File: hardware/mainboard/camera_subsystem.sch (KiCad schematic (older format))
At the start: 12 parts

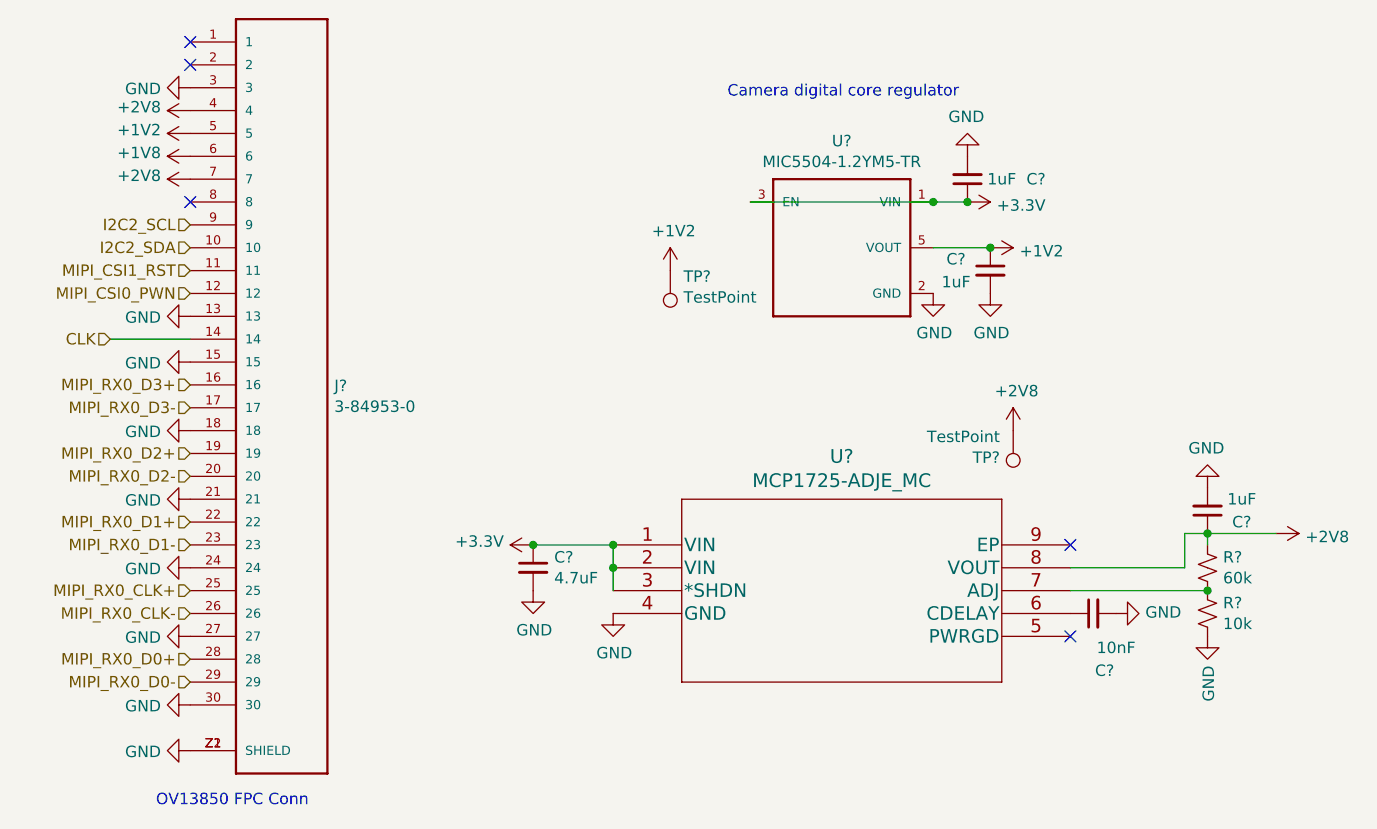
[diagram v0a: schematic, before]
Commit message: finish sch arch, remove coproc, add bl driver, need to do TC power supply
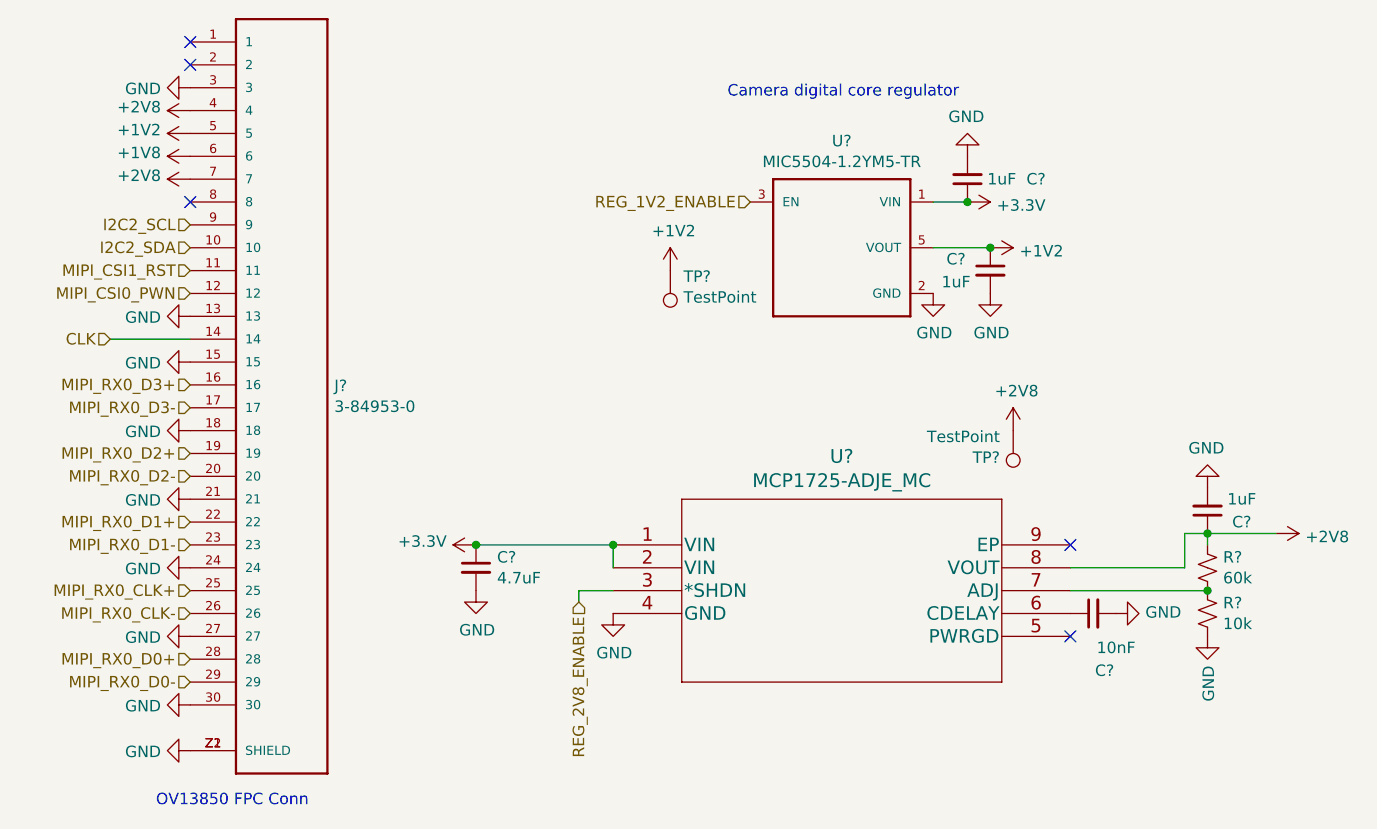
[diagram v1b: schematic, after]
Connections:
- net +3V3: no longer U?.3 (*SHDN), U?.3 (EN)
- new net REG_1V2_ENABLE: U?.3 (EN)
- new net REG_2V8_ENABLE: U?.3 (*SHDN)
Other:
- moved on the sheet: C?
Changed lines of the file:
@@
 	1    0    0    -1
 $EndComp
-Connection ~ 6150 1900
-Wire Wire Line
-	5350 1900 6150 1900
 $Comp
 L power:GND #PWR?
@@
 L power:GND #PWR?
 U 1 1 600090EF
-P 4400 3600
+P 4150 3600
 AR Path="/600090EF" Ref="#PWR?"  Part="1"
 AR Path="/5FFAA2CE/600090EF" Ref="#PWR?"  Part="1"
-F 0 "#PWR?" H 4400 3350 50  0001 C CNN
-F 1 "GND" H 4405 3427 50  0000 C CNN
-F 2 "" H 4400 3600 50  0001 C CNN
-F 3 "" H 4400 3600 50  0001 C CNN
-	1    4400 3600
+F 0 "#PWR?" H 4150 3350 50  0001 C CNN
+F 1 "GND" H 4155 3427 50  0000 C CNN
+F 2 "" H 4150 3600 50  0001 C CNN
+F 3 "" H 4150 3600 50  0001 C CNN
+	1    4150 3600
 	1    0    0    -1
 $EndComp
@@
 L Device:C_Small C?
 U 1 1 600090F5
-P 4400 3500
+P 4150 3500
 AR Path="/600090F5" Ref="C?"  Part="1"
 AR Path="/5FFAA2CE/600090F5" Ref="C?"  Part="1"
-F 0 "C?" H 4492 3546 50  0000 L CNN
-F 1 "4.7uF" H 4492 3455 50  0000 L CNN
-F 2 "Capacitor_SMD:C_0402_1005Metric_Pad0.74x0.62mm_HandSolder" H 4400 3500 50  0001 C CNN
-F 3 "~" H 4400 3500 50  0001 C CNN
-	1    4400 3500
+F 0 "C?" H 4242 3546 50  0000 L CNN
+F 1 "4.7uF" H 4242 3455 50  0000 L CNN
+F 2 "Capacitor_SMD:C_0402_1005Metric_Pad0.74x0.62mm_HandSolder" H 4150 3500 50  0001 C CNN
+F 3 "~" H 4150 3500 50  0001 C CNN
+	1    4150 3500
 	1    0    0    -1
 $EndComp
@@
 $EndComp
 Wire Wire Line
-	4750 3500 4750 3600
-Connection ~ 4750 3500
-Wire Wire Line
 	4750 3400 4750 3500
-$Comp
-L mainboard:MCP1725-ADJE_MC U?
-U 1 1 60009112
-P 4750 3400
-AR Path="/60009112" Ref="U?"  Part="1"
-AR Path="/5FFAA2CE/60009112" Ref="U?"  Part="1"
-F 0 "U?" H 5750 3787 60  0000 C CNN
-F 1 "MCP1725-ADJE_MC" H 5750 3681 60  0000 C CNN
-F 2 "mainboard:MCP1725-ADJE_MC" H 5750 3640 60  0001 C CNN
-F 3 "" H 4750 3400 60  0000 C CNN
-	1    4750 3400
-	1    0    0    -1
-$EndComp
 $Comp
 L power:GND #PWR?
@@
 L power:+3.3V #PWR?
 U 1 1 60009124
-P 4400 3400
+P 4150 3400
 AR Path="/60009124" Ref="#PWR?"  Part="1"
 AR Path="/5FFAA2CE/60009124" Ref="#PWR?"  Part="1"
-F 0 "#PWR?" H 4400 3250 50  0001 C CNN
-F 1 "+3.3V" V 4415 3528 50  0000 L CNN
-F 2 "" H 4400 3400 50  0001 C CNN
-F 3 "" H 4400 3400 50  0001 C CNN
-	1    4400 3400
+F 0 "#PWR?" H 4150 3250 50  0001 C CNN
+F 1 "+3.3V" V 4165 3528 50  0000 L CNN
+F 2 "" H 4150 3400 50  0001 C CNN
+F 3 "" H 4150 3400 50  0001 C CNN
+	1    4150 3400
 	0    -1   -1   0
 $EndComp
-Wire Wire Line
-	4400 3400 4750 3400
-Connection ~ 4400 3400
-Connection ~ 4750 3400
+Connection ~ 4150 3400
 Wire Wire Line
 	6750 3600 7350 3600
@@
 Text HLabel 2900 2000 0    50   Input ~ 0
 I2C2_SCL
+$Comp
+L mainboard:MCP1725-ADJE_MC U?
+U 1 1 60009112
+P 4750 3400
+AR Path="/60009112" Ref="U?"  Part="1"
+AR Path="/5FFAA2CE/60009112" Ref="U?"  Part="1"
+F 0 "U?" H 5750 3787 60  0000 C CNN
+F 1 "MCP1725-ADJE_MC" H 5750 3681 60  0000 C CNN
+F 2 "mainboard:MCP1725-ADJE_MC" H 5750 3640 60  0001 C CNN
+F 3 "" H 4750 3400 60  0000 C CNN
+	1    4750 3400
+	1    0    0    -1
+$EndComp
+Wire Wire Line
+	4150 3400 4750 3400
+Connection ~ 4750 3400
+Wire Wire Line
+	4600 3650 4600 3600
+Wire Wire Line
+	4600 3600 4750 3600
+Text HLabel 4600 3650 3    50   Input ~ 0
+REG_2V8_ENABLE
+Text HLabel 5350 1900 0    50   Input ~ 0
+REG_1V2_ENABLE
 $EndSCHEMATC

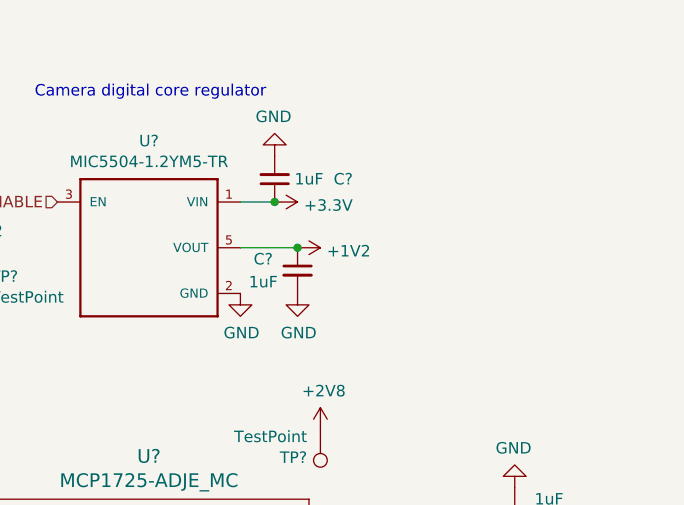
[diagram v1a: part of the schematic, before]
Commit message: finish basic schematic, need to decide audio situation
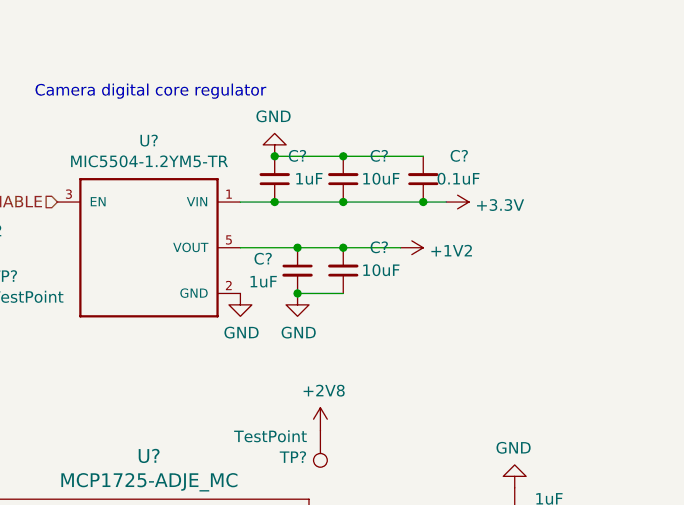
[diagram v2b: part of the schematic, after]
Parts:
- added C? (x2): 10uF, symbol Device:C_Small
- added C?: 0.1uF, symbol Device:C_Small
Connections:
- net +1V2: now also C?.2
- net +3V3: now also C?.1, C?.1
- net GND: now also C?.1, C?.2, C?.2
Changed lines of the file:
@@
 $Descr A4 11693 8268
 encoding utf-8
-Sheet 6 7
+Sheet 3 7
 Title ""
 Date ""
@@
 L power:+3.3V #PWR?
 U 1 1 5FFF5446
-P 6300 1900
+P 7050 1900
 AR Path="/5FFF5446" Ref="#PWR?"  Part="1"
 AR Path="/5FFAA2CE/5FFF5446" Ref="#PWR?"  Part="1"
-F 0 "#PWR?" H 6300 1750 50  0001 C CNN
-F 1 "+3.3V" V 6315 2028 50  0000 L CNN
-F 2 "" H 6300 1900 50  0001 C CNN
-F 3 "" H 6300 1900 50  0001 C CNN
-	1    6300 1900
+F 0 "#PWR?" H 7050 1750 50  0001 C CNN
+F 1 "+3.3V" V 7065 2028 50  0000 L CNN
+F 2 "" H 7050 1900 50  0001 C CNN
+F 3 "" H 7050 1900 50  0001 C CNN
+	1    7050 1900
 	0    1    1    0
 $EndComp
@@
 AR Path="/5FFF544C" Ref="C?"  Part="1"
 AR Path="/5FFAA2CE/5FFF544C" Ref="C?"  Part="1"
-F 0 "C?" H 6000 1800 50  0000 C CNN
+F 0 "C?" H 6200 1700 50  0000 C CNN
 F 1 "1uF" H 6150 1800 50  0000 C CNN
 F 2 "Capacitor_SMD:C_0402_1005Metric_Pad0.74x0.62mm_HandSolder" H 6300 1800 50  0001 C CNN
@@
 Wire Wire Line
 	6150 1900 6300 1900
-Connection ~ 6300 1900
 $Comp
 L power:GND #PWR?
@@
 L power:+1V2 #PWR?
 U 1 1 5FFF546D
-P 6400 2100
+P 6850 2100
 AR Path="/5FFF546D" Ref="#PWR?"  Part="1"
 AR Path="/5FFAA2CE/5FFF546D" Ref="#PWR?"  Part="1"
-F 0 "#PWR?" H 6400 1950 50  0001 C CNN
-F 1 "+1V2" V 6415 2228 50  0000 L CNN
-F 2 "" H 6400 2100 50  0001 C CNN
-F 3 "" H 6400 2100 50  0001 C CNN
-	1    6400 2100
-	0    1    1    0
-$EndComp
-Connection ~ 6400 2100
+F 0 "#PWR?" H 6850 1950 50  0001 C CNN
+F 1 "+1V2" V 6865 2228 50  0000 L CNN
+F 2 "" H 6850 2100 50  0001 C CNN
+F 3 "" H 6850 2100 50  0001 C CNN
+	1    6850 2100
+	0    1    1    0
+$EndComp
 Text Notes 5250 1450 0    50   ~ 0
 Camera digital core regulator\n
@@
 Text HLabel 5350 1900 0    50   Input ~ 0
 REG_1V2_ENABLE
+$Comp
+L Device:C_Small C?
+U 1 1 6021847C
+P 6600 2200
+AR Path="/5FF71A49/6021847C" Ref="C?"  Part="1"
+AR Path="/5FFAA2CE/6021847C" Ref="C?"  Part="1"
+F 0 "C?" H 6400 2100 50  0000 L CNN
+F 1 "10uF" H 6350 2200 50  0000 L CNN
+F 2 "" H 6600 2200 50  0001 C CNN
+F 3 "~" H 6600 2200 50  0001 C CNN
+	1    6600 2200
+	-1   0    0    1
+$EndComp
+Wire Wire Line
+	6600 2100 6850 2100
+Wire Wire Line
+	6600 2100 6400 2100
+Connection ~ 6600 2100
+Connection ~ 6400 2100
+Wire Wire Line
+	6600 2300 6400 2300
+Connection ~ 6400 2300
+$Comp
+L Device:C_Small C?
+U 1 1 6021FE8A
+P 6600 1800
+AR Path="/5FF71A49/6021FE8A" Ref="C?"  Part="1"
+AR Path="/5FFAA2CE/6021FE8A" Ref="C?"  Part="1"
+F 0 "C?" H 6400 1700 50  0000 L CNN
+F 1 "10uF" H 6350 1800 50  0000 L CNN
+F 2 "" H 6600 1800 50  0001 C CNN
+F 3 "~" H 6600 1800 50  0001 C CNN
+	1    6600 1800
+	-1   0    0    1
+$EndComp
+Wire Wire Line
+	6600 1700 6300 1700
+Connection ~ 6300 1700
+Wire Wire Line
+	6600 1900 6300 1900
+Connection ~ 6300 1900
+$Comp
+L Device:C_Small C?
+U 1 1 60225ABF
+P 6950 1800
+AR Path="/5FF71A49/60225ABF" Ref="C?"  Part="1"
+AR Path="/5FFAA2CE/60225ABF" Ref="C?"  Part="1"
+F 0 "C?" H 6750 1700 50  0000 L CNN
+F 1 "0.1uF" H 6700 1800 50  0000 L CNN
+F 2 "" H 6950 1800 50  0001 C CNN
+F 3 "~" H 6950 1800 50  0001 C CNN
+	1    6950 1800
+	-1   0    0    1
+$EndComp
+Wire Wire Line
+	6600 1700 6950 1700
+Connection ~ 6600 1700
+Wire Wire Line
+	7050 1900 6950 1900
+Connection ~ 6600 1900
+Connection ~ 6950 1900
+Wire Wire Line
+	6950 1900 6600 1900
 $EndSCHEMATC
